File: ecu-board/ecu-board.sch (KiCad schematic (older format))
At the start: 6 parts, among them J1 MicroSquirt_connector

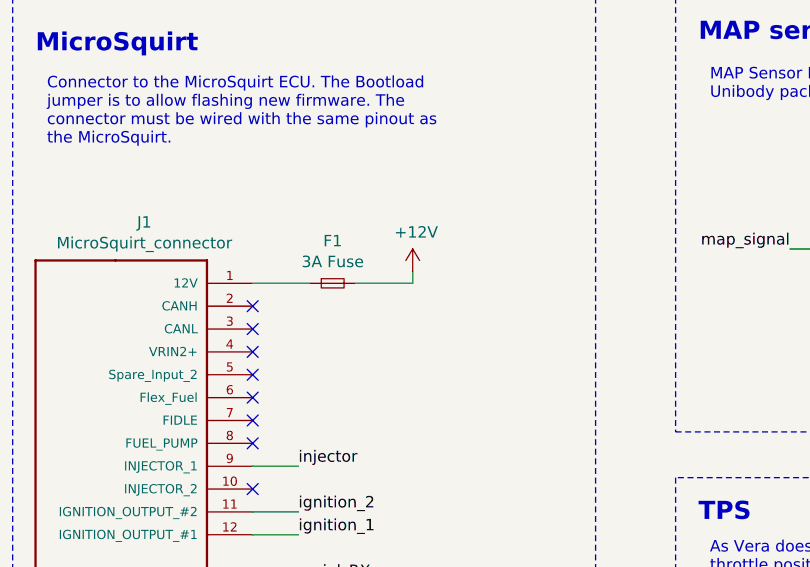
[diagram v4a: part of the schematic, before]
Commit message: Added indicator LEDs to fuses. Resolves #15.
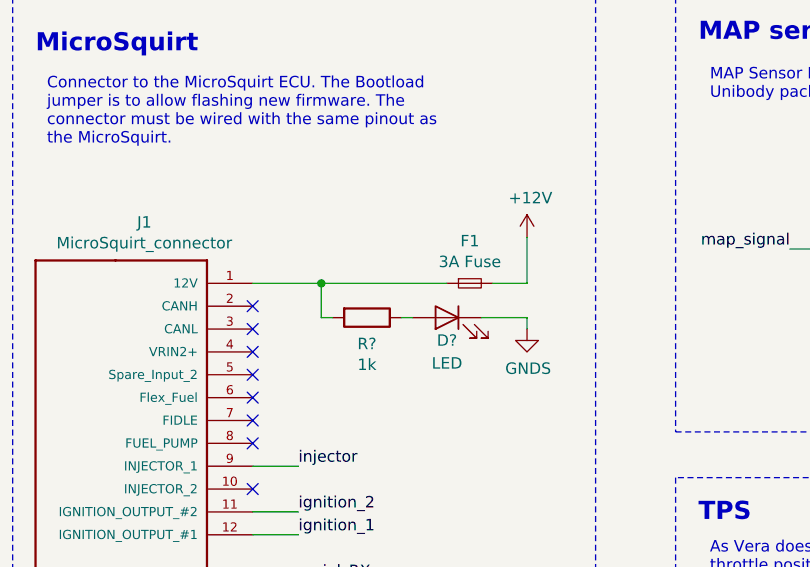
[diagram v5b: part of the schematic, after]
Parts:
- added D?: LED, LEDs:LED_D3.0mm, symbol Device:LED
- added R?: 1k, symbol Device:R
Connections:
- net GNDS: now also D?.1 (K)
- net at F1.1, J1.1 (12V): now also R?.2
- new net: D?.2 (A), R?.1
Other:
- moved on the sheet: F1
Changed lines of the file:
@@
 L Device:Fuse_Small F1
 U 1 1 5C5C2E0F
-P 2600 2300
-F 0 "F1" H 2600 2485 50  0000 C CNN
-F 1 "3A Fuse" H 2600 2394 50  0000 C CNN
-F 2 "" H 2600 2300 50  0001 C CNN
-F 3 "~" H 2600 2300 50  0001 C CNN
-F 4 "2292904" H 2600 2300 50  0001 C CNN "Farnell"
-	1    2600 2300
-	1    0    0    -1
-$EndComp
-Wire Wire Line
-	2250 2300 2500 2300
+P 3200 2300
+F 0 "F1" H 3200 2485 50  0000 C CNN
+F 1 "3A Fuse" H 3200 2394 50  0000 C CNN
+F 2 "" H 3200 2300 50  0001 C CNN
+F 3 "~" H 3200 2300 50  0001 C CNN
+F 4 "2292904" H 3200 2300 50  0001 C CNN "Farnell"
+	1    3200 2300
+	1    0    0    -1
+$EndComp
 $Comp
 L power:+12V #PWR01
 U 1 1 5C5C2EC1
-P 2950 2250
-F 0 "#PWR01" H 2950 2100 50  0001 C CNN
-F 1 "+12V" H 2965 2423 50  0000 C CNN
-F 2 "" H 2950 2250 50  0001 C CNN
-F 3 "" H 2950 2250 50  0001 C CNN
-	1    2950 2250
-	1    0    0    -1
-$EndComp
-Wire Wire Line
-	2700 2300 2950 2300
-Wire Wire Line
-	2950 2300 2950 2250
+P 3450 2100
+F 0 "#PWR01" H 3450 1950 50  0001 C CNN
+F 1 "+12V" H 3465 2273 50  0000 C CNN
+F 2 "" H 3450 2100 50  0001 C CNN
+F 3 "" H 3450 2100 50  0001 C CNN
+	1    3450 2100
+	1    0    0    -1
+$EndComp
 $Comp
 L Device:Jumper_NO_Small JP1
@@
 	1    0    0    -1
 $EndComp
+$Comp
+L Device:LED D?
+U 1 1 5CA86402
+P 3100 2450
+F 0 "D?" H 3100 2350 50  0000 C CNN
+F 1 "LED" H 3100 2250 50  0000 C CNN
+F 2 "LEDs:LED_D3.0mm" H 3100 2450 50  0001 C CNN
+F 3 "~" H 3100 2450 50  0001 C CNN
+F 4 "2251296" H 3100 2450 50  0001 C CNN "Farnell"
+	1    3100 2450
+	-1   0    0    -1
+$EndComp
+$Comp
+L Device:R R?
+U 1 1 5CA87A75
+P 2750 2450
+F 0 "R?" V 2865 2450 50  0000 C CNN
+F 1 "1k" V 2956 2450 50  0000 C CNN
+F 2 "" V 2680 2450 50  0001 C CNN
+F 3 "~" H 2750 2450 50  0001 C CNN
+	1    2750 2450
+	0    1    1    0
+$EndComp
+Wire Wire Line
+	3450 2100 3450 2300
+Wire Wire Line
+	3300 2300 3450 2300
+$Comp
+L power:GNDS #PWR?
+U 1 1 5CB6A35F
+P 3450 2500
+F 0 "#PWR?" H 3450 2250 50  0001 C CNN
+F 1 "GNDS" H 3455 2327 50  0000 C CNN
+F 2 "" H 3450 2500 50  0001 C CNN
+F 3 "" H 3450 2500 50  0001 C CNN
+	1    3450 2500
+	1    0    0    -1
+$EndComp
+Wire Wire Line
+	2250 2300 2550 2300
+Wire Wire Line
+	3250 2450 3450 2450
+Wire Wire Line
+	3450 2450 3450 2500
+Wire Wire Line
+	2900 2450 2950 2450
+Wire Wire Line
+	2600 2450 2550 2450
+Wire Wire Line
+	2550 2450 2550 2300
+Wire Wire Line
+	3100 2300 2550 2300
+Connection ~ 2550 2300
 $EndSCHEMATC
